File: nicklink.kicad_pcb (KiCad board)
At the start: 2 copper layers, 33.2 x 28.8 mm, 42 parts, among them J1 Conn_02x10_Odd_Even, J2 USB_C_Receptacle_USB2.0_16P, J3 Conn_02x10_Odd_Even, SW1 RESET, SW2 BOOT0, U1 STM32F103C8T6, U2 TLV75533PDRV, U3 USBLC6-2P6, U4 LSM6DSV16X, Y1 8MHz

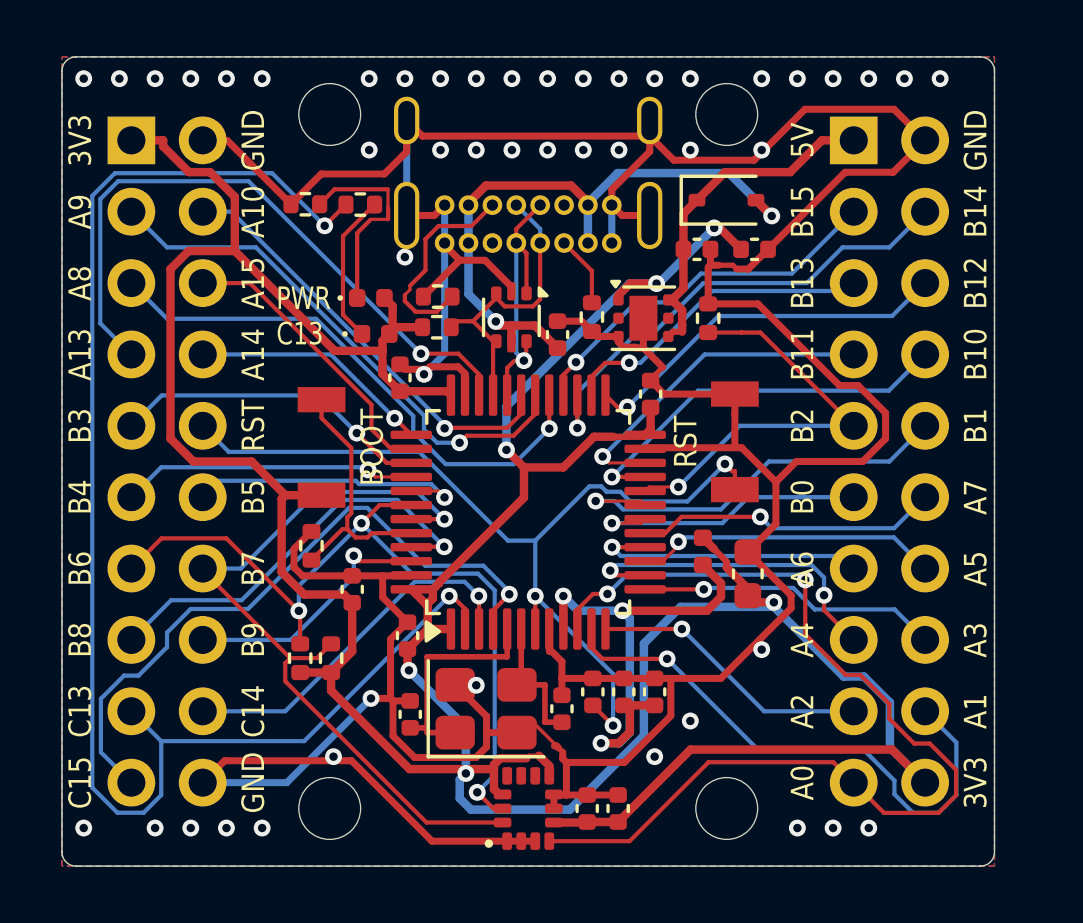
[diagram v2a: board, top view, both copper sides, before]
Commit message: v1.3: JLCPCB design rules, IMU moved into existing gaps (25.5 mm tall)
JLCPCB 2-layer + Economic PCBA limits are now enforced by DRC
(board setup + nicklink.kicad_dru): 0.18 mm component annular ring,
0.15 mm SMD pad-to-pad, 0.45 mm pad hole-to-hole, 0.5 mm plated slots,
0.3 mm copper-to-edge, 0.15 mm silk-to-pad, 0.10 mm mask web,
1.0 mm / 0.15 mm silkscreen text and lines.

Changes to comply:
- USB4085 pads 0.36 mm hole / 0.72 mm pad (was 0.40/0.70 = 0.15 ring),
  shield pads +0.06 mm
- pin labels 1.0 mm tall; label strips 1.2 -> 1.4 mm; all silk >= 0.15 mm
- back legend reflowed to clear the mounting holes

The IMU now sits in the right channel below RESET (caps beneath it), the
ferrite in the MCU courtyard notch, the bulk cap in the top-left pocket and
the I2C pull-ups beside PB6/PB7, so the board returns to 25.5 mm tall:
33.99 x 25.5 mm (867 mm^2, -23% vs v1.1). Routed via seed 13.

Also: board template is now tracked (tools/board_template.kicad_pcb),
tools/route_try.sh for the seed search, docs/README JLC section.

ERC 0/0; DRC 0 violations, 0 unconnected, 0 parity issues.

Co-Authored-By: Claude Opus 5.5 <noreply@anthropic.com>
Claude-Session: https://claude.ai/code/session_01KPMtzubqGeBFaq48UcVZaf
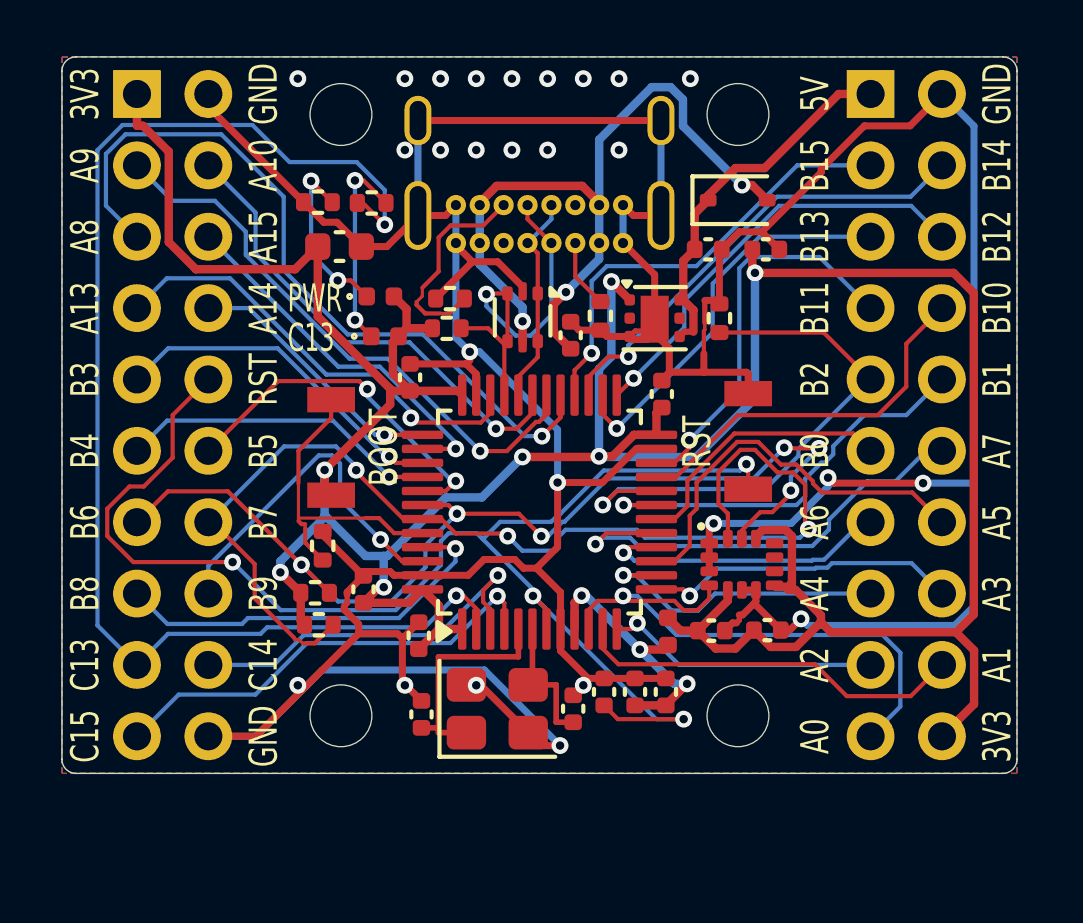
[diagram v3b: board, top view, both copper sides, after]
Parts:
- moved C5 18.6 mm to (109.9, 106.8), turned to 0 degrees
- moved U4 11.5 mm to (124.2, 118.1), turned to 0 degrees
- moved C15 8.28 mm to (125.1, 120.4), turned to 0 degrees
- moved C14 7.72 mm to (123.1, 120.4), turned to 0 degrees
- moved H3 3.32 mm to (109.9, 123.5)
- moved H4 3.32 mm to (124.1, 123.5)
- moved FB1 3.11 mm to (121.6, 120.4)
- moved R7 2.39 mm to (109.0, 119.1), turned to 0 degrees
- moved J1 1.76 mm to (128.8, 101.3)
- moved J3 1.66 mm to (102.7, 101.3)
- moved R9 1.27 mm to (109.1, 120.2), turned to 0 degrees
- moved SW1 0.47 mm to (124.4, 113.7)
- moved C13 0.47 mm to (118.1, 109.9)
- moved R3 0.45 mm to (109.1, 105.2)
- moved R5 0.44 mm to (113.8, 108.6)
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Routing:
- net /NRST: track 32.9 -> 49.3 mm, vias 3 -> 4
- net /PA0: track 36.6 -> 20.2 mm, vias 2 -> 1
- net +3.3V: track 137.3 -> 123.6 mm, vias 6 -> 7
- net /PB7: track 28.2 -> 40.3 mm, vias 1 -> 3
- net GND: track 169.3 -> 179.7 mm, vias 47 -> 26
- net /PB6: track 29.1 -> 37.1 mm, vias 3 -> 6
- net +3.3VA: track 17.5 -> 9.59 mm
- net /PC15: track 23.9 -> 16.2 mm
- net /PA8: track 19.6 -> 26.9 mm
- net /PA13: track 23.3 -> 16.1 mm
- net /PA1: track 20.1 -> 13.9 mm, vias 1 -> 0
- net /PA7: track 10.8 -> 16.5 mm
- net VBUS: track 22.5 -> 27.8 mm, vias 2 -> 3
- net /PC13: track 51.9 -> 47.0 mm
- net /PB2: track 14.9 -> 19.7 mm
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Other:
- board size 33.2 x 28.8 mm -> 34 x 25.5 mm
- board text added: "5V max 5.5V, 3V3 250mA"
- board text added: "C13 LED, low = on"
- board text added: "IMU 0x6A INT1 = A0"
- board text removed: "3V3 out: 250 mA max"
- board text removed: "5V: USB out/<=5.5V in"
- board text removed: "C13 LED (low=on)"
- board text removed: "I2C1 B6/B7, INT1 A0"
- board text removed: "IMU LSM6DSV16X 0x6A"
- board text removed: "STM32F103C8 8MHz"

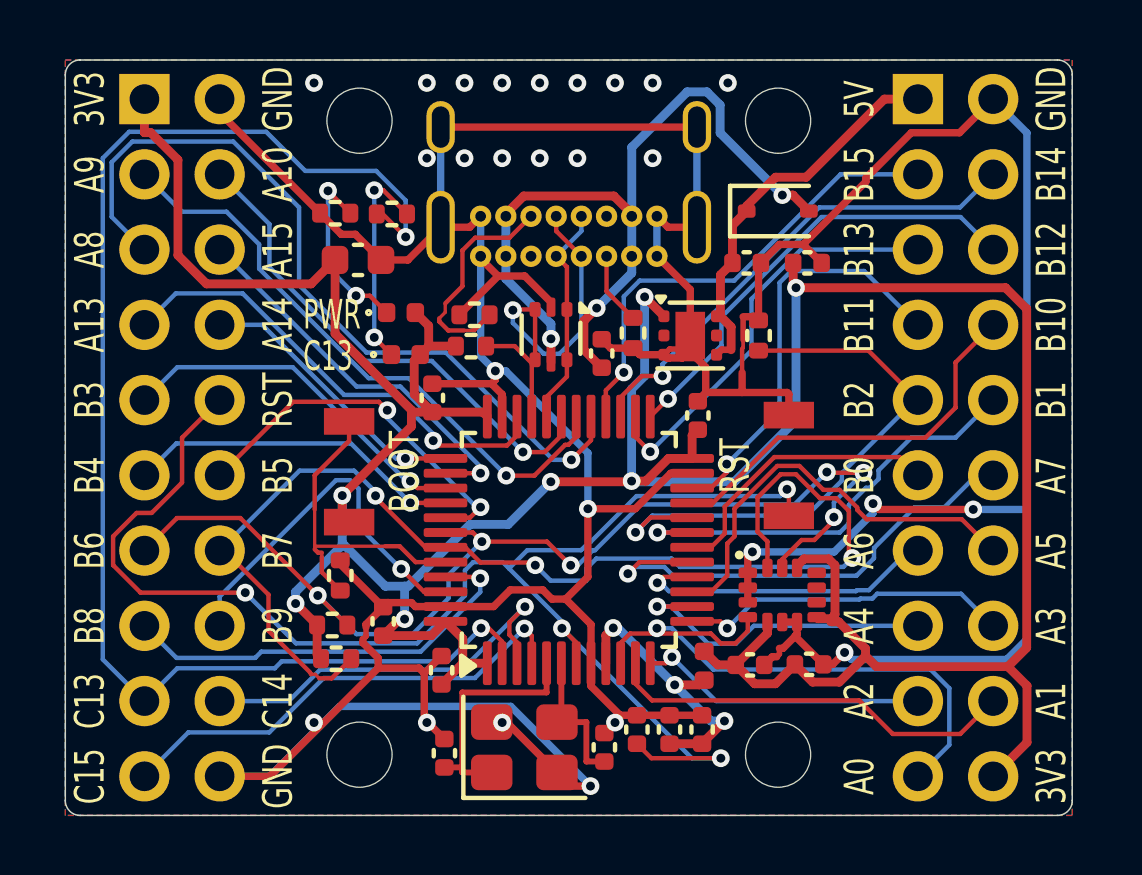
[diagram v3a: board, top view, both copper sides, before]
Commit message: v1.3: fix the five-reviewer audit findings
Independent reviews (power, MCU, USB, IMU/headers, fab/DFM) found issues that
would have made the board fail or be unreliable. Fixed:

- CPL: per-footprint JLC rotation corrections (LQFP-48 -90, SOT-666 +180,
  LGA-14 +180), verified against JLC's EasyEDA footprints. As shipped, U1
  would have been rotated 90 deg and U3 would have shorted VBUS to GND.
- LDO: output cap C8 now 0.95 mm from OUT; C12 -> 10 uF 0603; two 0.3 mm
  thermal vias in the exposed pad (project WSON footprint).
- IMU INT1 (forced low at power-up) now reaches A0 through R10 10k.
- USB4085: 0.38 mm holes / 0.74 mm pads (inside GCT's 0.40 +-0.05 spec,
  JLC 0.18 mm ring), thermal-relief GND pins.
- IMU: no pour under the body, pre-routed local fan-out (GND vias, 3V3 rail,
  B.Cu GND link under the MCU); OCS_Aux/SDO_Aux tied to VDDIO.
- VDDA caps next to the VDDA pin; MCU group 0.25 mm left so fan-out vias fit.
- Docs: PB6/PB7 and NRST are 3.3 V only, I2C pull-ups to 3.3 V only, ENIG,
  hardware/back-feed notes; review summary in docs/REVIEW.md.
- Tooling: pour-only rule areas no longer exported as DSN keepouts; B.Cu
  pre-routes and pre-placed vias; stitching respects oval slots.

ERC 0/0; DRC 0 violations, 0 unconnected, 0 parity issues.

Co-Authored-By: Claude Opus 5.5 <noreply@anthropic.com>
Claude-Session: https://claude.ai/code/session_01KPMtzubqGeBFaq48UcVZaf
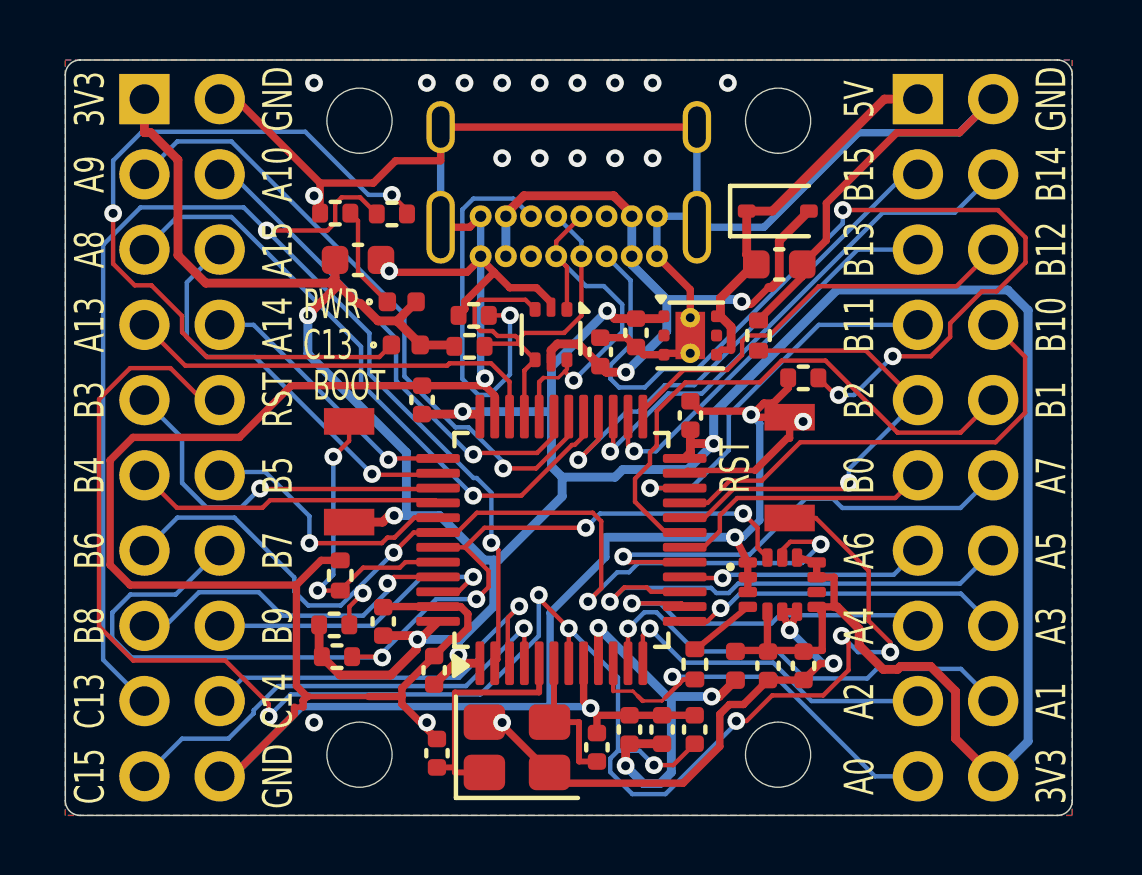
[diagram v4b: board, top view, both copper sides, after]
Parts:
- added R10: 10k, Resistor_SMD:R_0402_1005Metric, F.Cu at (121.2, 120.4)
- C12: value 1u -> 10u; footprint Capacitor_SMD:C_0402_1005Metric -> Capacitor_SMD:C_0603_1608Metric
- U2: footprint Package_SON:WSON-6-1EP_2x2mm_P0.65mm_EP1x1.6mm -> nicklink:WSON-6-1EP_2x2mm_P0.65mm_EP1x1.6mm_ThermalVias03
- moved C8 6.25 mm to (119.3, 109.2), turned to -90 degrees
- moved R4 5.94 mm to (124.9, 110.7), turned to 0 degrees
- moved C9 1.95 mm to (121.2, 122.6)
- moved C7 1.35 mm to (120.1, 122.6)
- moved C6 1.35 mm to (119.0, 122.6)
- moved C12 1.10 mm to (124.1, 106.9)
- moved FB1 1.06 mm to (122.6, 120.5)
- moved C14 0.61 mm to (123.7, 120.5), turned to -90 degrees
- moved D1 0.36 mm to (111.4, 108.2)
- moved C3 0.35 mm to (112.0, 111.5)
- moved U4 0.35 mm to (124.2, 117.7)
- moved D3 0.32 mm to (111.5, 109.6)
- moved C1 0.25 mm to (112.5, 120.6)
- moved C10 0.25 mm to (112.5, 123.4)
- moved C11 0.25 mm to (117.9, 123.2)
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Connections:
- U4 pad 10: unconnected-(U4-OCS_Aux-Pad10) -> +3.3V
- U4 pad 11: unconnected-(U4-SDO_Aux-Pad11) -> +3.3V
- U4 pad 4: /PA0 -> /IMU_INT1
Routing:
- net /USB_CC1: track 2.45 -> 32.2 mm, vias 0 -> 3
- net /USER_LED_K: track 7.23 -> 26.2 mm
- net /NRST: track 49.3 -> 62.7 mm, vias 4 -> 7
- net GND: track 179.7 -> 189.8 mm
- net /PA0: track 20.2 -> 14.1 mm
- net /USB_CC2: track 7.56 -> 13.3 mm, vias 0 -> 1
- net /PB7: track 40.3 -> 34.7 mm, vias 3 -> 4
- net /PA8: track 26.9 -> 21.4 mm
- net /USB_D-: track 7.55 -> 12.8 mm, vias 0 -> 1
- net VBUS: track 27.8 -> 23.0 mm, vias 3 -> 2
- net /PB1: track 14.9 -> 19.0 mm, vias 1 -> 0
- net /PB2: track 19.7 -> 15.9 mm
- net +3.3VA: track 9.59 -> 13.4 mm
- net /PB6: track 37.1 -> 33.6 mm, vias 6 -> 4
- net /PB5: track 12.8 -> 9.31 mm, vias 2 -> 1
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
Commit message: v1.3 reliability pass: protected power path, STM32 best practices, SPICE + emulated test firmware
Power: R12 1R anti-surge in series with VBUS (hot-plug ring 6.1-11.4 V -> 5.38 V
at LDO IN, inrush 33 uC); C12 4.7 uF, 3V3 10 uF bulk removed; F1 0.5 A PTC + Q1
DMP2165UW reverse-polarity FET on the J1.1 5V pin branch.
STM32: 4.7 uF on VDD3 (DS5319 Fig. 14); D+ pull-up from VBUS (R2 2k2 + R11 4k7,
AN4879 3.1.1) so J1.1 power no longer back-feeds the host; R6 330R user LED.
Layout: locked USB-C orientation ties, VBUS path U3 -> C13 -> J2, IMU GND return
via its caps, GND vias for R3/VSS_2; seed 12 baked, finished with the new
tools/fixroute.sh grid router. stitch.py checks connectivity per pour island
(tools/gndnet.py). DRC 0/0/0, ERC 0/0.
sim/: ngspice benches 1-11 (as-built table in results/summary.md).
firmware/: bare-metal bring-up firmware + Renode board model, 10 tests pass.

Co-Authored-By: Claude Opus 5.5 <noreply@anthropic.com>
Claude-Session: https://claude.ai/code/session_01KPMtzubqGeBFaq48UcVZaf
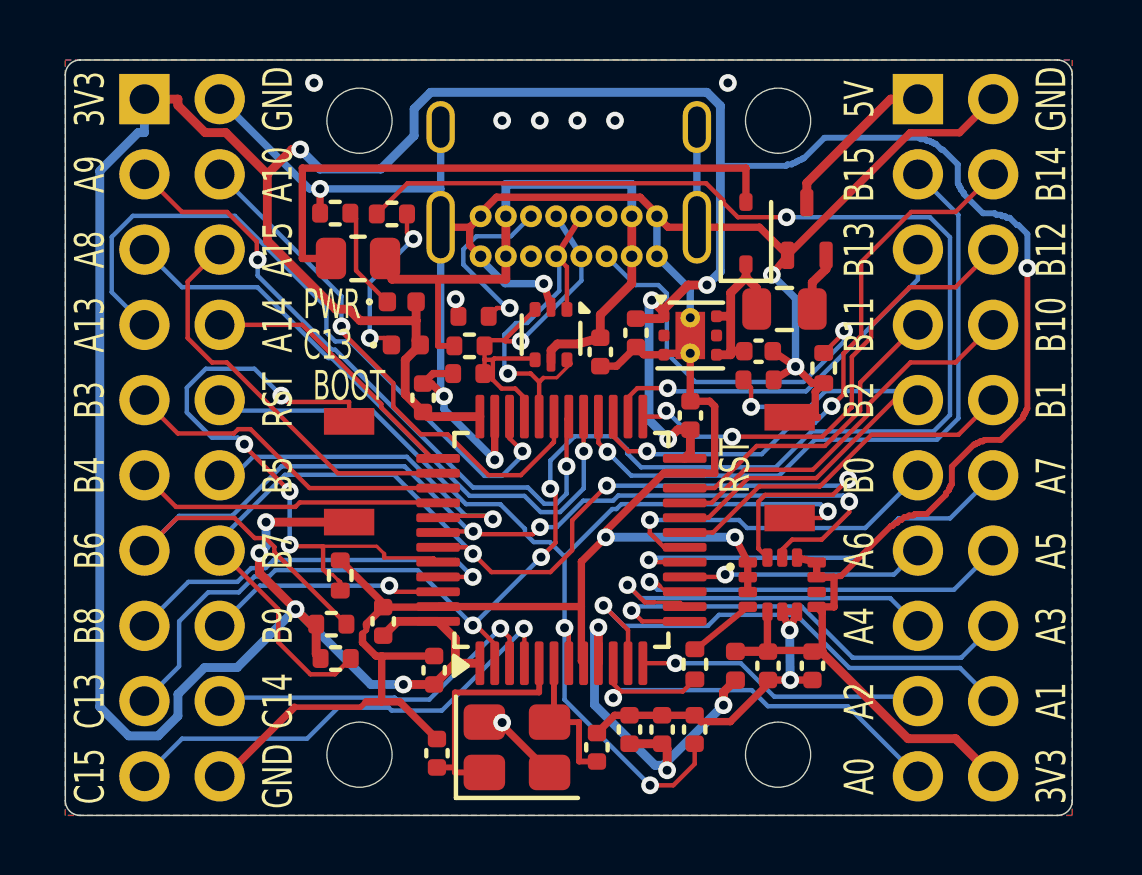
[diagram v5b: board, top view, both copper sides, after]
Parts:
- removed C5: 10u, Capacitor_SMD:C_0603_1608Metric
- added F1: 0.5A, Fuse:Fuse_0805_2012Metric, F.Cu at (124.3, 108.4)
- added Q1: DMP2165UW, nicklink:SOT-323_SC-70_NoSilk, F.Cu at (125.0, 105.7)
- added R11: 4k7, nicklink:R_0402_1005Metric_NoSilk, F.Cu at (113.6, 110.6)
- added R12: 1R, Resistor_SMD:R_0805_2012Metric, F.Cu at (109.9, 106.7)
- C12: value 10u -> 4u7; footprint Capacitor_SMD:C_0603_1608Metric -> Capacitor_SMD:C_0402_1005Metric
- C4: value 100n -> 4u7
- R2: value 1k5 -> 2k2
- R5, R8: footprint Resistor_SMD:R_0402_1005Metric -> nicklink:R_0402_1005Metric_NoSilk
- R6: value 1k5 -> 330
- moved C12 3.01 mm to (123.4, 109.8)
- moved R8 1.50 mm to (123.4, 110.8), turned to 0 degrees
- moved D2 1.31 mm to (123.0, 105.8), turned to 90 degrees
- moved R4 0.76 mm to (125.6, 110.4), turned to 90 degrees
- moved C15 0.30 mm to (125.2, 120.5)
- moved R7 0.10 mm to (109.0, 119.0)
- moved C3 0.08 mm to (112.1, 111.4)
- moved R9 0.08 mm to (109.1, 120.2)
- turned C13 to -90 degrees
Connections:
- C12 pad 1: +5V -> /VSYS
- D2 pad 1: +5V -> /VSYS
- D2 pad 2: VBUS -> /VBUS_D
- R2 pad 1: +3.3V -> VBUS
- U2 pad 4: +5V -> /VSYS
- U2 pad 6: +5V -> /VSYS
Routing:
- net GND: track 189.8 -> 132.3 mm, vias 26 -> 18
- net +3.3V: track 121.2 -> 150.0 mm, vias 7 -> 9
- net /NRST: track 62.7 -> 37.7 mm, vias 7 -> 3
- net /USER_LED_K: track 26.2 -> 5.71 mm
- net /VBUS_D: track 0.00 -> 20.1 mm
- net /PC13: track 45.1 -> 64.7 mm, vias 2 -> 4
- net /USB_CC1: track 32.2 -> 12.9 mm, vias 3 -> 1
- net /BOOT0: track 10.6 -> 21.3 mm, vias 2 -> 4
- net /PA13: track 14.4 -> 23.5 mm, vias 0 -> 1
- net +5V: track 13.5 -> 5.59 mm
- net /USB_CC2: track 13.3 -> 6.27 mm
- net /PB1: track 19.0 -> 12.3 mm
- net /PB6: track 33.6 -> 40.0 mm, vias 4 -> 3
- net /VSYS: track 0.00 -> 5.90 mm
- net /PB15: track 17.2 -> 23.1 mm
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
